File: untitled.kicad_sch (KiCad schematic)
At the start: 3 parts

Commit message: V0.1
really jjust updating a bunch of stuff
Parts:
- added C?: 10uF, symbol Device:C_Polarized
- added J?: 5V, symbol Connector:Jack-DC
- added R?: 2k, symbol Device:R
- added SW? (x15): ~, symbol NidecSwitches:TR2-21-L
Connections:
- net +3.3V: now also U?.25 (DCPRG)
- net GND: now also U?.3 (VPRG), C?.2, J?.2, R?.2, SW?.4, SW?.4, SW?.4, SW?.4, SW?.4, SW?.4, SW?.4, SW?.4, SW?.4, SW?.4, SW?.4, SW?.4, SW?.4, SW?.4, SW?.4
- net SCLK: now reaches U?.1 (SCLK)
- net at U?.10 (OUT6): now also SW?.6
- net at U?.11 (OUT7): now also SW?.6
- net at U?.14 (OUT8): now also SW?.6
- net at U?.15 (OUT9): now also SW?.6
- net at U?.16 (OUT10): now also SW?.6
- net at U?.17 (OUT11): now also SW?.6
- net at U?.18 (OUT12): now also SW?.6
- net at U?.19 (OUT13): now also SW?.6
- net SIN: now reaches U?.2 (SIN)
- net at U?.20 (OUT14): now also SW?.6
- net at U?.21 (OUT15): now also SW?.6
- net GSCLK: now reaches U?.24 (GSCLK)
- net at U?.26 (IREF): now also R?.1
- net BLANK: now reaches U?.31 (BLANK)
- net XLAT: now reaches U?.32 (XLAT)
- net at U?.5 (OUT1): now also SW?.6
- net at U?.6 (OUT2): now also SW?.6
- net at U?.7 (OUT3): now also SW?.6
- net at U?.8 (OUT4): now also SW?.6
- net at U?.9 (OUT5): now also SW?.6
- net at U?.16 (I15): now also SW?.2
- net at U?.17 (I14): now also SW?.2
- net at U?.18 (I13): now also SW?.2
- net at U?.19 (I12): now also SW?.2
- net at U?.2 (I7): now also SW?.2
- net at U?.20 (I11): now also SW?.2
- net at U?.21 (I10): now also SW?.2
- net at U?.22 (I9): now also SW?.2
- net at U?.23 (I8): now also SW?.2
- net at U?.3 (I6): now also SW?.2
- net at U?.4 (I5): now also SW?.2
- net at U?.5 (I4): now also SW?.2
- net at U?.6 (I3): now also SW?.2
- net at U?.7 (I2): now also SW?.2
- net at U?.8 (I1): now also SW?.2
- net 2V renamed +5V
- net +5V: now also C?.1, J?.1, SW?.5, SW?.5, SW?.5, SW?.5, SW?.5, SW?.5, SW?.5, SW?.5, SW?.5, SW?.5, SW?.5, SW?.5, SW?.5, SW?.5, SW?.5
- no-connect marks 1 -> 3
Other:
- note added: "Center + Jack size 5"
- note added: "MODE pulled GND for PWM mode"
- note added: "Power from SWI3-5-N-P5"
- title: (none) -> VMC-1
- moved on the sheet: SW?, U?

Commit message: First Round ERC Checks
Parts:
- gave numbers to parts that had none: 20
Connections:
- no-connect marks 3 -> 35

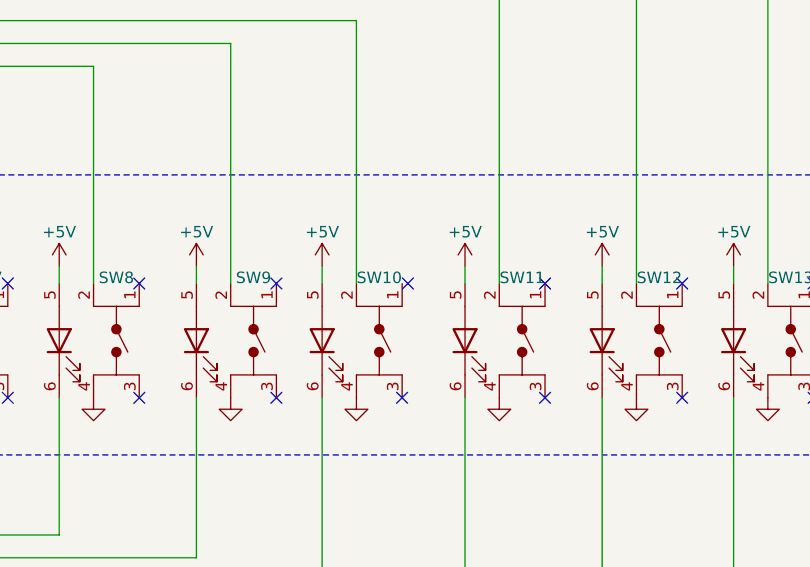
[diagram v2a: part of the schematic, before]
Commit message: ERC Fixes
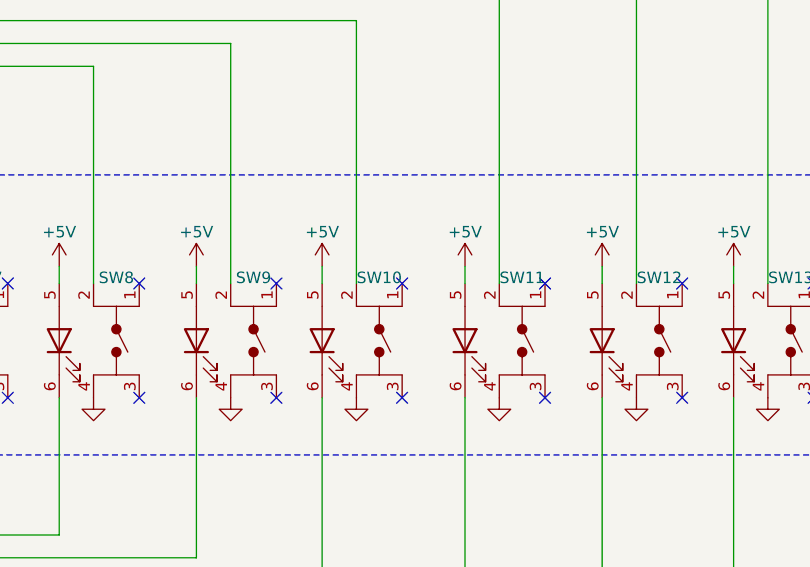
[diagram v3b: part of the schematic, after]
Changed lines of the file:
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@@
   (no_connect (at 93.98 123.825))
   (no_connect (at 139.065 123.825))
-  (no_connect (at 153.67 111.125))
+  (no_connect (at 153.035 111.125))
   (no_connect (at 78.74 123.825))
   (no_connect (at 93.98 111.125))

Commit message: Post Kicad Community Telling Me Shit is Wrong
way more stuff needs love, DECOUPERS DUMA88s
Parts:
- added C2: C, symbol Device:C
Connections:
- net +3.3V: now also C2.1
- net GND: now also U5.15 (~{E}), C2.2
- no-connect marks 35 -> 34
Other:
- note added: "MAX DC PER DRIVER IS 120mA!!!"
- note added: "NEED BIGGER DRIVER"
- note added: "Needs A Decoupler"
- note added: "SHOULD ALSO POWER TEENSY AND SLICE THING ON BOTTOM"
- moved on the sheet: C1, J1, R1, SW10, SW11, SW12, SW13, SW14, SW15, SW16, SW17, SW2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
